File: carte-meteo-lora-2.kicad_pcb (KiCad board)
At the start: 4 copper layers, 80 parts, among them J1 USB_C_Receptacle_USB2.0_14P, J2 Conn_Coaxial, J3 Conn_Coaxial, J4 Conn_Coaxial, J5 Conn_01x04_Pin, SW1 SW_Push, SW2 SW_Push, U1 HS96L03W2C03, U2 SX1262TR8-GC, U3 LDL212PV33R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

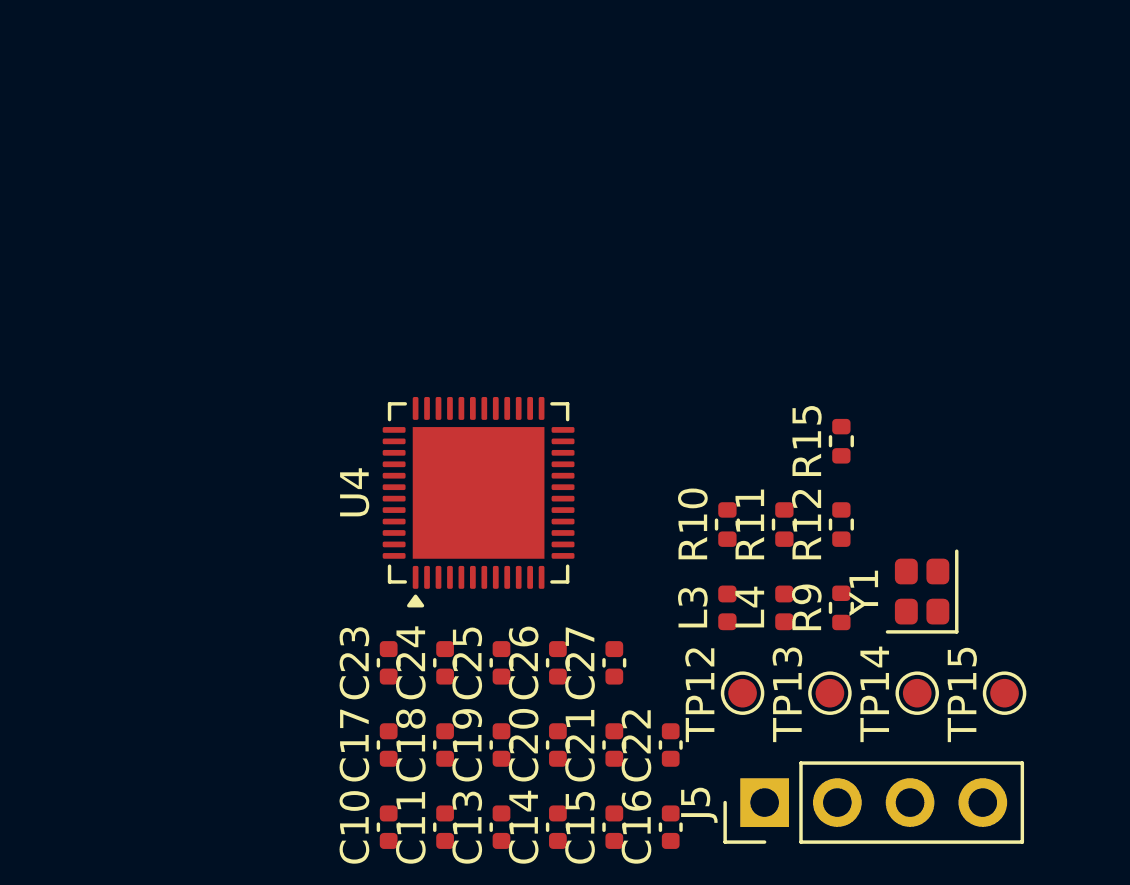
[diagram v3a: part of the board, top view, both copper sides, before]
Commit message: pcb: add initial crystal layout
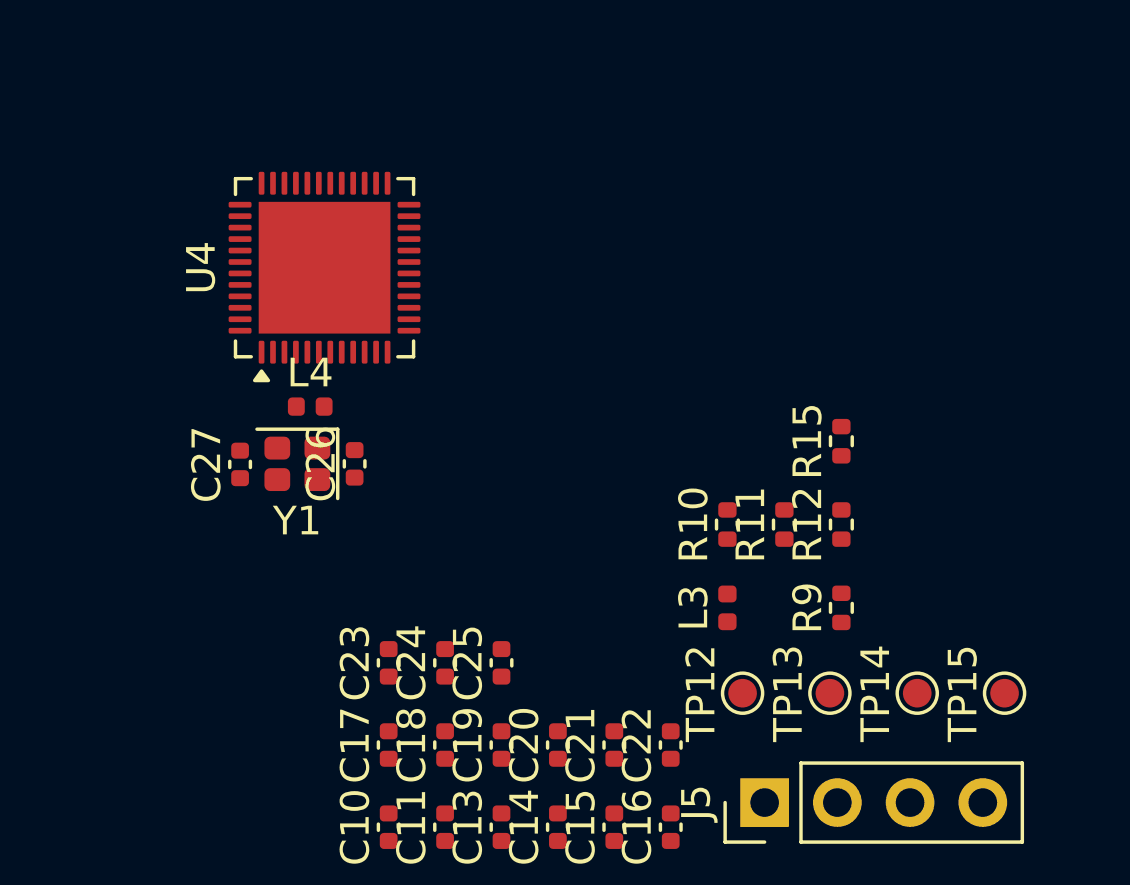
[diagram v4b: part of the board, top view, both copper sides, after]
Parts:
- moved Y1 22.3 mm to (90.0, 77.3), turned to 180 degrees
- moved L4 18.0 mm to (90.5, 75.3), turned to 0 degrees
- moved C27 14.8 mm to (88.0, 77.3)
- moved C26 9.94 mm to (92.0, 77.3)
- moved U4 9.53 mm to (91.0, 70.5)
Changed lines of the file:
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@@
 	(footprint "Package_DFN_QFN:QFN-48-1EP_6x6mm_P0.4mm_EP4.6x4.6mm"
 		(layer "F.Cu")
-		(at 96.33 78.315 90)
+		(at 90.95 70.45 90)
 		(descr "QFN, 48 Pin (http://infocenter.nordicsemi.com/pdf/nRF51822_PS_v3.3.pdf#page=67)")
 		(tags "QFN NoLead")
@@
 	(footprint "Crystal:Crystal_SMD_2016-4Pin_2.0x1.6mm"
 		(layer "F.Cu")
-		(at 111.82 81.76 90)
+		(at 90 77.3 180)
 		(descr "SMD2016/4, Crystal, 2.0x1.6mm package, SMD, http://www.q-crystal.com/upload/5/2015552223166229.pdf")
 		(property "Reference" "Y1"
-			(at 0 -2 90)
+			(at 0 -2 0)
 			(layer "F.SilkS")
 			(effects
@@
 		)
 		(property "Value" "48M"
-			(at 0 2 90)
+			(at 0 2 0)
 			(layer "F.Fab")
 			(effects
@@
 		)
 		(property "Datasheet" ""
-			(at 0 0 90)
+			(at 0 0 0)
 			(layer "F.Fab")
 			(hide yes)
@@
 		)
 		(property "Description" "Four pin crystal, GND on pins 2 and 4"
-			(at 0 0 90)
+			(at 0 0 0)
 			(layer "F.Fab")
 			(hide yes)
@@
 		)
 		(property "KiLib_Generator" "crystal_resonator_oscillator"
-			(at 0 0 90)
+			(at 0 0 0)
 			(layer "F.SilkS")
 			(hide yes)
@@
 		)
 		(property "Manufacturer" "TROQ"
-			(at 0 0 90)
+			(at 0 0 180)
 			(unlocked yes)
 			(layer "F.Fab")
@@
 		)
 		(property "Manufacturer Part Number" "R940000096"
-			(at 0 0 90)
+			(at 0 0 180)
 			(unlocked yes)
 			(layer "F.Fab")
@@
 		)
 		(property "Basic" "X"
-			(at 0 0 90)
+			(at 0 0 180)
 			(unlocked yes)
 			(layer "F.Fab")
@@
 		)
 		(property "JLCPCB Part #" "C7206306"
-			(at 0 0 90)
+			(at 0 0 180)
 			(unlocked yes)
 			(layer "F.Fab")
@@
 		(duplicate_pad_numbers_are_jumpers no)
 		(fp_line
-			(start -1.41 -1.21)
-			(end -1.41 1.21)
+			(start -1.41 1.21)
+			(end 1.41 1.21)
 			(stroke
 				(width 0.12)
@@
 		)
 		(fp_line
-			(start -1.41 1.21)
-			(end 1.41 1.21)
+			(start -1.41 -1.21)
+			(end -1.41 1.21)
 			(stroke
 				(width 0.12)
@@
 		)
 		(fp_text user "${REFERENCE}"
-			(at 0 0 90)
+			(at 0 0 0)
 			(layer "F.Fab")
 			(effects
@@
 		)
 		(pad "1" smd roundrect
-			(at -0.7 0.55 90)
+			(at -0.7 0.55 180)
 			(size 0.9 0.8)
 			(layers "F.Cu" "F.Mask" "F.Paste")
@@
 		)
 		(pad "2" smd roundrect
-			(at 0.7 0.55 90)
+			(at 0.7 0.55 180)
 			(size 0.9 0.8)
 			(layers "F.Cu" "F.Mask" "F.Paste")
@@
 		)
 		(pad "3" smd roundrect
-			(at 0.7 -0.55 90)
+			(at 0.7 -0.55 180)
 			(size 0.9 0.8)
 			(layers "F.Cu" "F.Mask" "F.Paste")
@@
 		)
 		(pad "4" smd roundrect
-			(at -0.7 -0.55 90)
+			(at -0.7 -0.55 180)
 			(size 0.9 0.8)
 			(layers "F.Cu" "F.Mask" "F.Paste")
@@
 	(footprint "Inductor_SMD:L_0402_1005Metric"
 		(layer "F.Cu")
-		(at 107.01 82.33 90)
+		(at 90.45 75.3)
 		(descr "Inductor SMD 0402 (1005 Metric), square (rectangular) end terminal, IPC-7351 nominal, (Body size source: http://www.tortai-tech.com/upload/download/2011102023233369053.pdf)")
 		(tags "inductor")
 		(property "Reference" "L4"
-			(at 0 -1.17 90)
+			(at 0 -1.17 0)
 			(layer "F.SilkS")
 			(effects
@@
 		)
 		(property "Value" "24n"
-			(at 0 1.17 90)
+			(at 0 1.17 0)
 			(layer "F.Fab")
 			(effects
@@
 		)
 		(property "Datasheet" ""
-			(at 0 0 90)
+			(at 0 0 0)
 			(layer "F.Fab")
 			(hide yes)
@@
 		)
 		(property "Description" "Inductor"
-			(at 0 0 90)
+			(at 0 0 0)
 			(layer "F.Fab")
 			(hide yes)
@@
 		)
 		(property "KiLib_Generator" "SMD_2terminal_chip_molded"
-			(at 0 0 90)
+			(at 0 0 0)
 			(layer "F.SilkS")
 			(hide yes)
@@
 		)
 		(property "Manufacturer" "Murata"
-			(at 0 0 90)
+			(at 0 0 0)
 			(unlocked yes)
 			(layer "F.Fab")
@@
 		)
 		(property "Manufacturer Part Number" "LQW15AN24NG00D"
-			(at 0 0 90)
+			(at 0 0 0)
 			(unlocked yes)
 			(layer "F.Fab")
@@
 		)
 		(property "Basic" "X"
-			(at 0 0 90)
+			(at 0 0 0)
 			(unlocked yes)
 			(layer "F.Fab")
@@
 		)
 		(property "JLCPCB Part #" "C167472"
-			(at 0 0 90)
+			(at 0 0 0)
 			(unlocked yes)
 			(layer "F.Fab")
@@
 		)
 		(fp_text user "${REFERENCE}"
-			(at 0 0 90)
+			(at 0 0 0)
 			(layer "F.Fab")
 			(effects
@@
 		)
 		(pad "1" smd roundrect
-			(at -0.485 0 90)
+			(at -0.485 0)
 			(size 0.59 0.64)
 			(layers "F.Cu" "F.Mask" "F.Paste")
@@
 		)
 		(pad "2" smd roundrect
-			(at 0.485 0 90)
+			(at 0.485 0)
 			(size 0.59 0.64)
 			(layers "F.Cu" "F.Mask" "F.Paste")
@@
 	(footprint "Capacitor_SMD:C_0402_1005Metric"
 		(layer "F.Cu")
-		(at 99.1 84.25 90)
+		(at 92 77.3 90)
 		(descr "Capacitor SMD 0402 (1005 Metric), square (rectangular) end terminal, IPC-7351 nominal, (Body size source: IPC-SM-782 page 76, https://www.pcb-3d.com/wordpress/wp-content/uploads/ipc-sm-782a_amendment_1_and_2.pdf)")
 		(tags "capacitor")
@@
 	(footprint "Capacitor_SMD:C_0402_1005Metric"
 		(layer "F.Cu")
-		(at 101.07 84.25 90)
+		(at 88 77.32 90)
 		(descr "Capacitor SMD 0402 (1005 Metric), square (rectangular) end terminal, IPC-7351 nominal, (Body size source: IPC-SM-782 page 76, https://www.pcb-3d.com/wordpress/wp-content/uploads/ipc-sm-782a_amendment_1_and_2.pdf)")
 		(tags "capacitor")

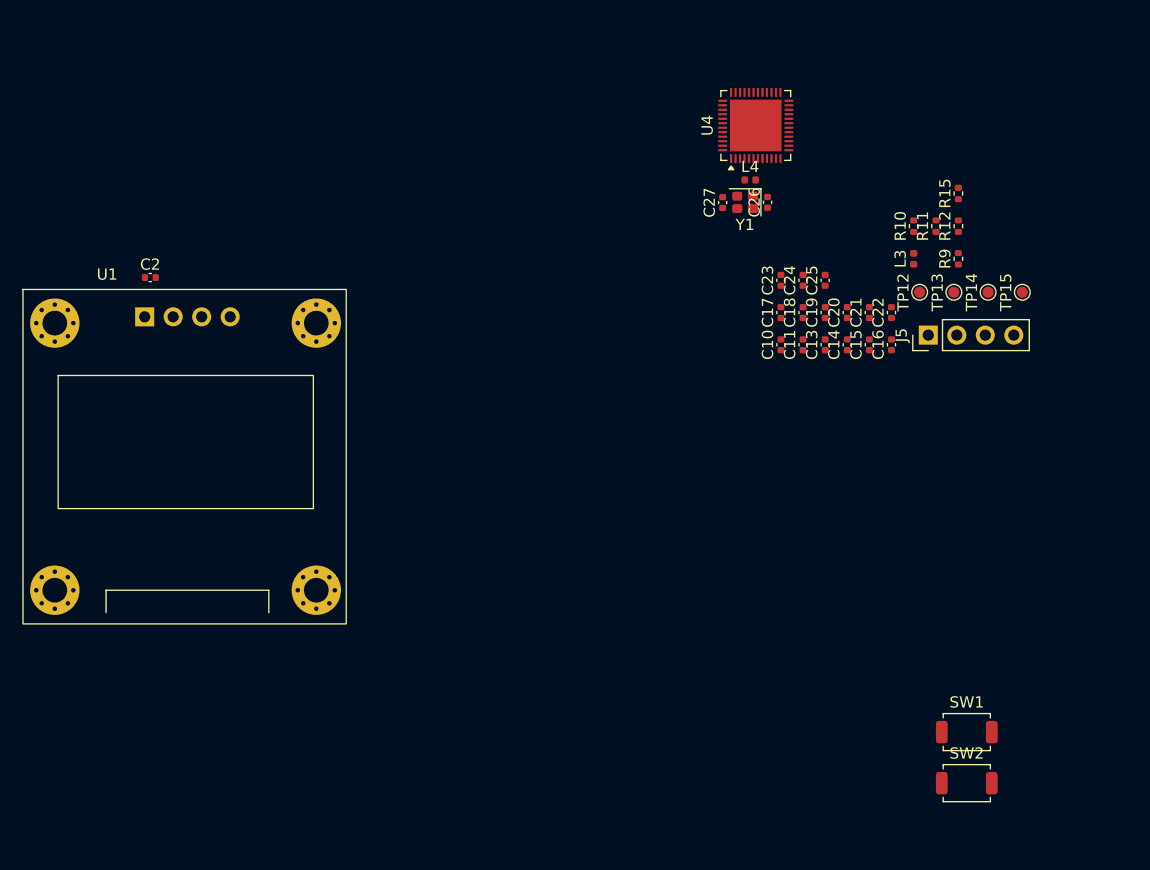
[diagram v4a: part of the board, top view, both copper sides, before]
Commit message: pcb: initial section
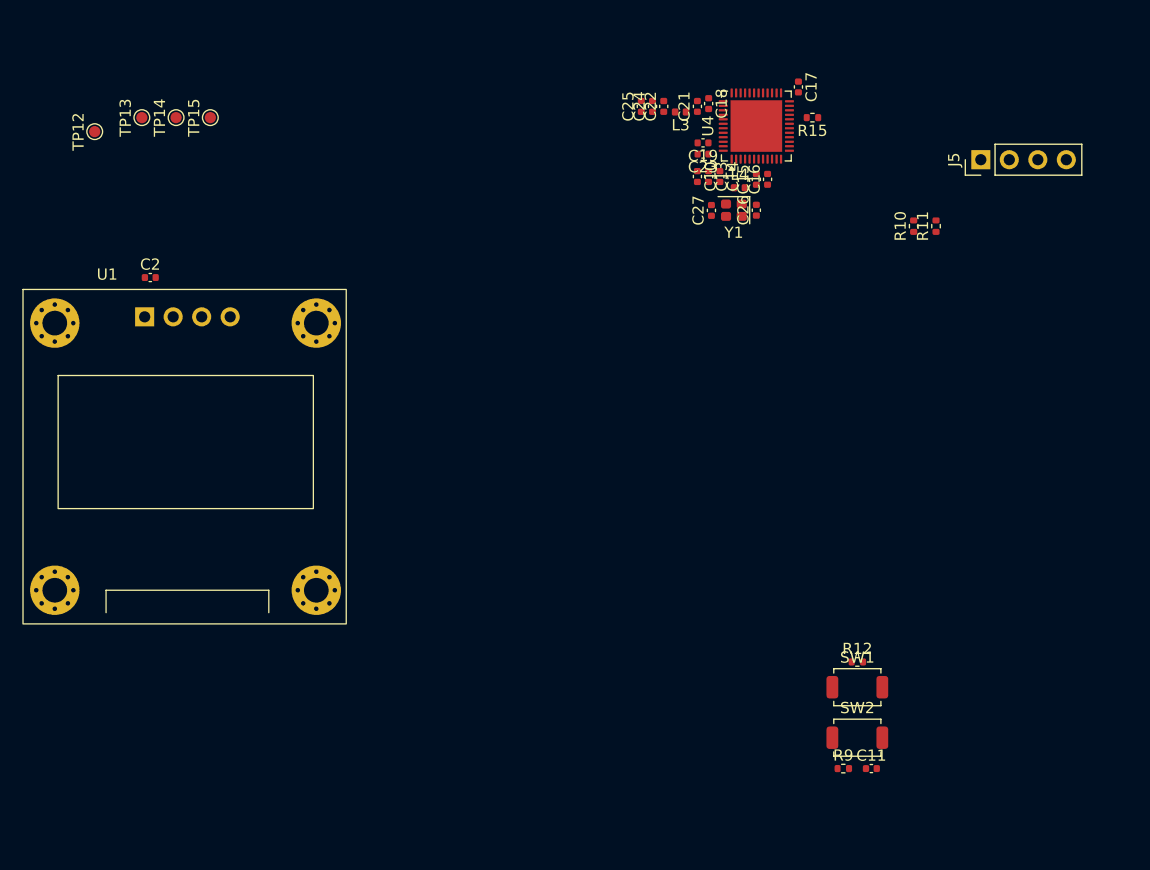
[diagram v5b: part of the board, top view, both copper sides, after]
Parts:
- removed C20: 10n, Capacitor_SMD:C_0402_1005Metric
- moved TP12 74.9 mm to (32.0, 71.0)
- moved TP14 74.0 mm to (39.3, 69.8)
- moved TP13 74.0 mm to (36.2, 69.8)
- moved TP15 74.0 mm to (42.4, 69.8)
- moved R9 46.6 mm to (98.8, 127.8), turned to 0 degrees
- moved R12 39.9 mm to (100.0, 118.2), turned to 0 degrees
- moved C11 38.2 mm to (101.2, 127.8), turned to 0 degrees
- moved C22 27.4 mm to (82.8, 68.8)
- moved L3 24.5 mm to (84.2, 69.2), turned to 180 degrees
- moved C21 23.9 mm to (85.8, 68.8)
- moved C25 22.6 mm to (80.8, 68.8)
- moved C24 20.5 mm to (81.8, 68.8)
- moved C18 20.4 mm to (86.8, 68.5), turned to -90 degrees
- moved C17 20.2 mm to (94.8, 67.0), turned to -90 degrees
- moved C14 18.8 mm to (87.8, 75.0), turned to -90 degrees
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
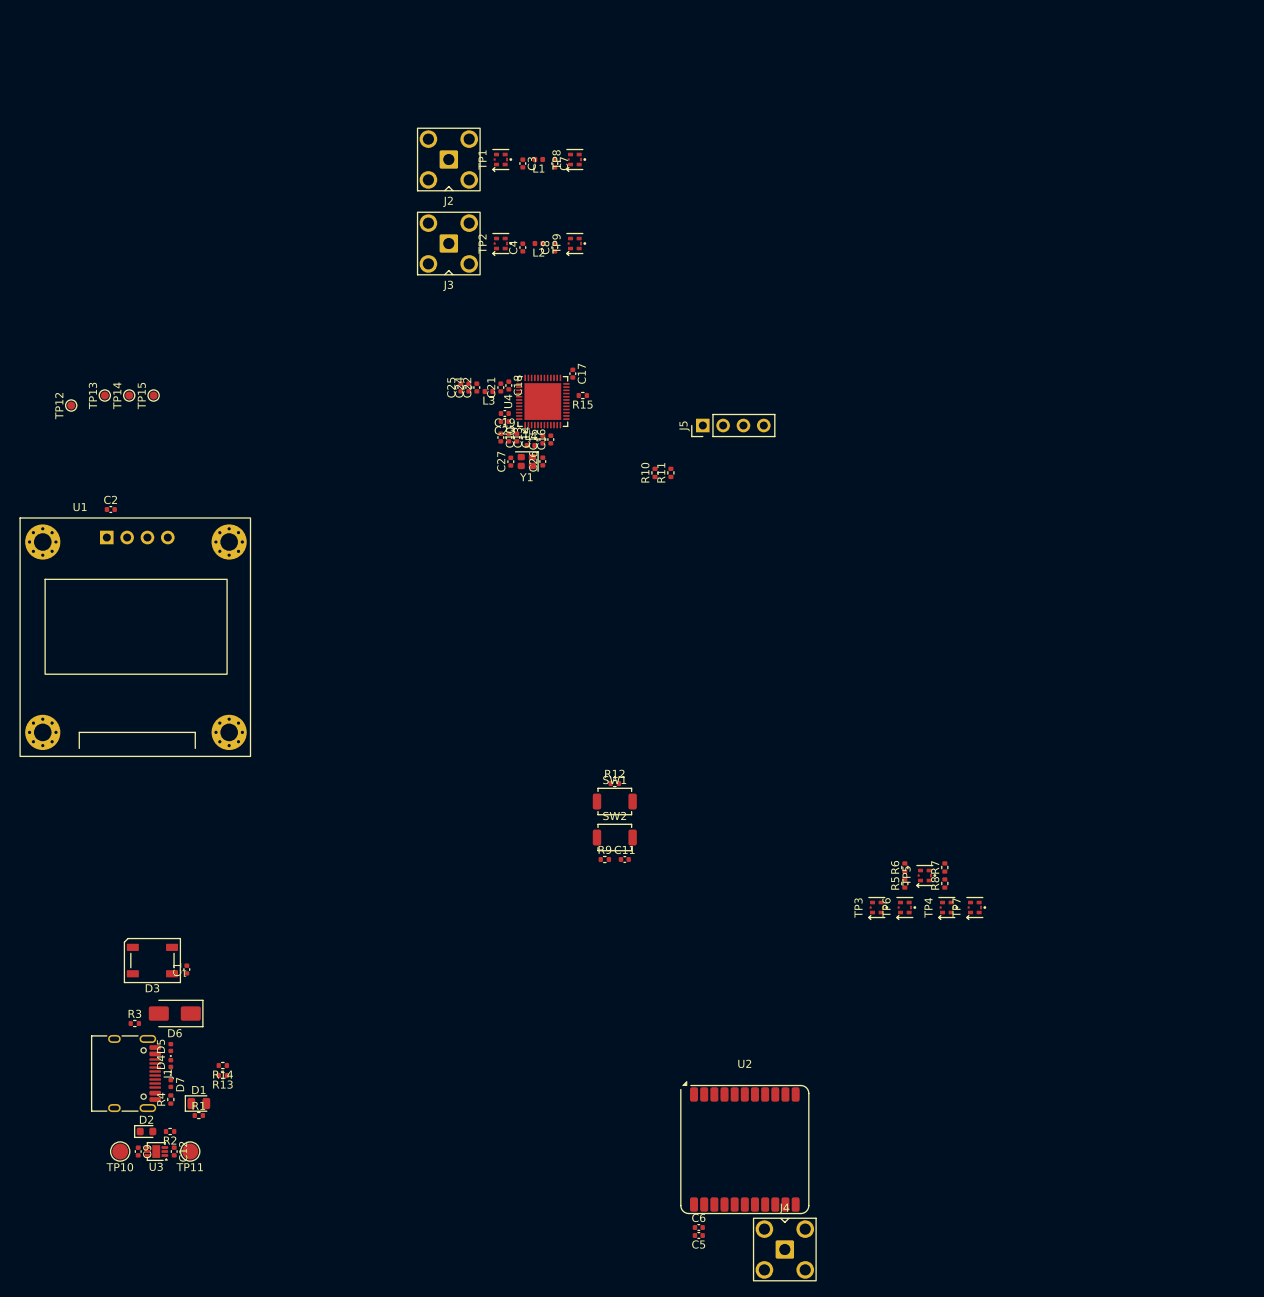
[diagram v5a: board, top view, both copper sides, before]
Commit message: pcb: add edge cut
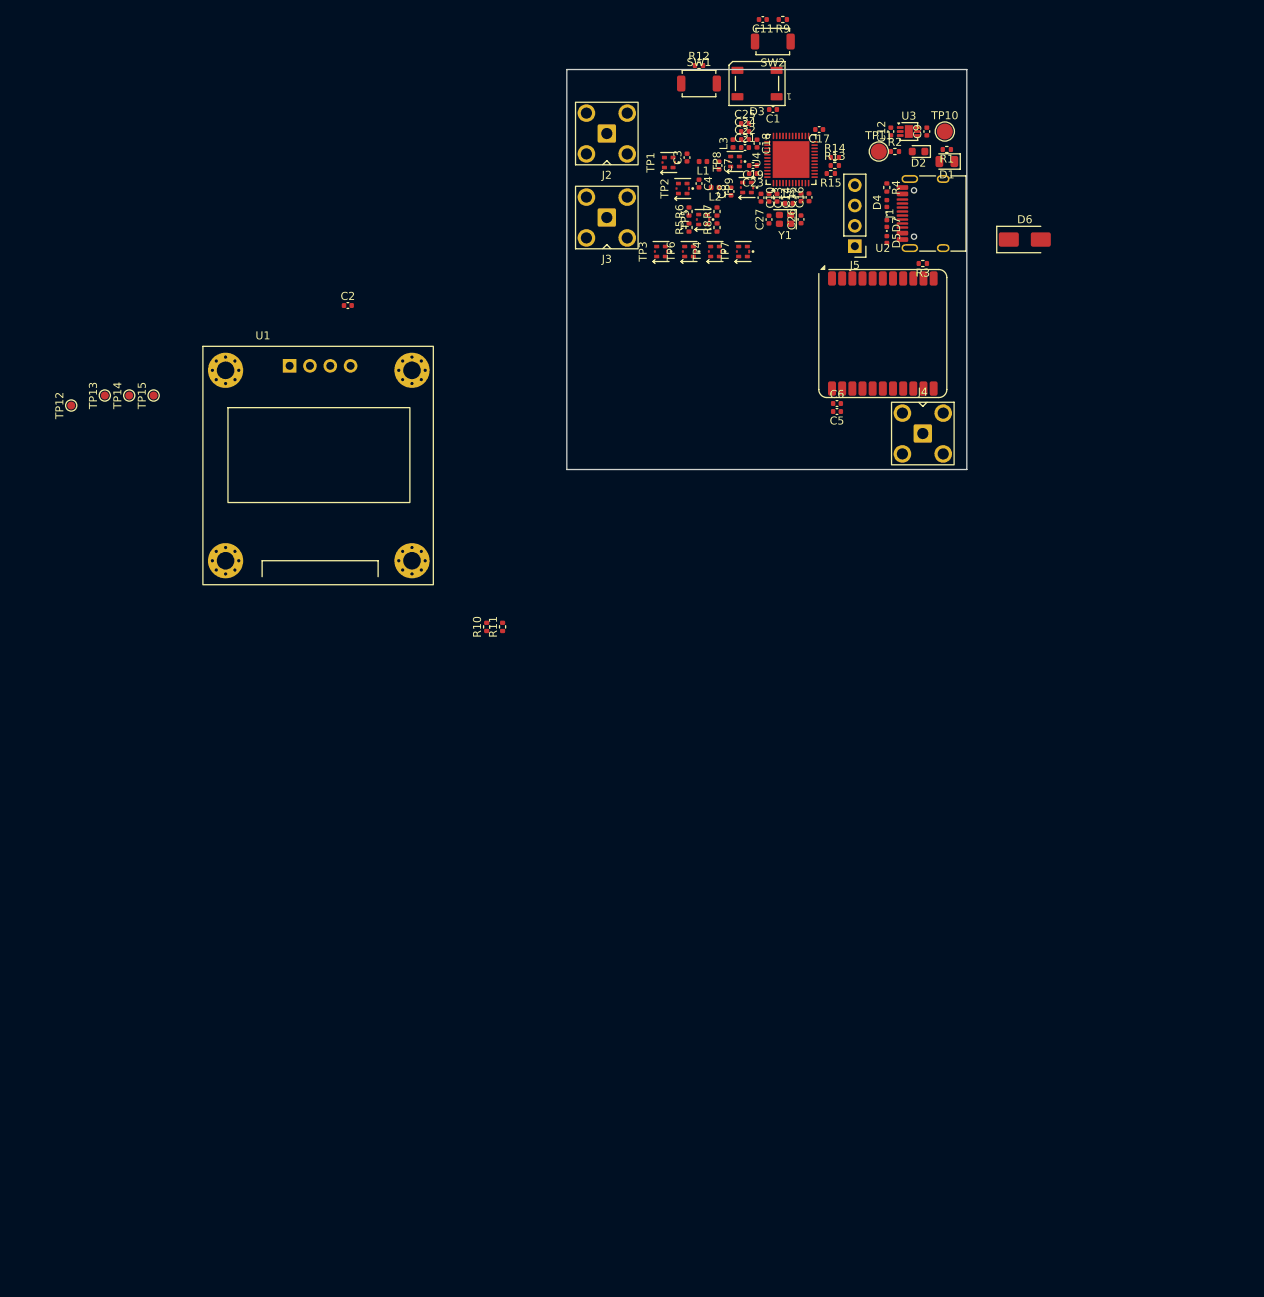
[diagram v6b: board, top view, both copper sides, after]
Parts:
- moved TP10 164.0 mm to (141.2, 36.8), turned to 0 degrees
- moved C9 161.2 mm to (139.0, 36.8), turned to 90 degrees
- moved U3 158.4 mm to (136.8, 36.8), turned to 0 degrees
- moved D2 155.9 mm to (138.0, 39.2), turned to 180 degrees
- moved C12 155.8 mm to (134.5, 36.8), turned to 90 degrees
- moved R1 152.7 mm to (141.5, 39.0), turned to 180 degrees
- moved R2 152.4 mm to (135.0, 39.2), turned to 0 degrees
- moved TP11 151.8 mm to (133.0, 39.2), turned to 0 degrees
- moved D1 150.4 mm to (141.5, 40.5), turned to 180 degrees
- moved J1 147.8 mm to (140.0, 47.0), turned to 90 degrees
- moved R4 144.9 mm to (134.0, 43.8), turned to -90 degrees
- moved D6 143.7 mm to (151.2, 50.2), turned to 0 degrees
- moved D4 139.9 mm to (134.0, 45.8)
- moved D7 139.9 mm to (134.0, 48.2)
- moved R13 137.1 mm to (127.5, 41.0), turned to 0 degrees
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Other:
- board outline added: 50 x 50 mm

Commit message: pcb: add m2 mouting holes
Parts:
- added H1: MountingHole_Pad, MountingHole:MountingHole_2.2mm_M2_Pad_Via, F.Cu at (177.0, 77.2)
- added H2: MountingHole_Pad, MountingHole:MountingHole_2.2mm_M2_Pad_Via, F.Cu at (177.0, 83.2)
